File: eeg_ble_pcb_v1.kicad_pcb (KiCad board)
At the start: 2 copper layers, 113 parts, among them J2 Conn_01x10_Socket, J3 Conn_01x10_Socket, J4 2171750001, Q1 FS8205, SW1 SW_Push, U1 STM32WB55RGVx, U2 TP4056-42-ESOP8, U3 ADS1299-4PAGR, U4 TPS61230DRC, U5 TPS63001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

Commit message: small pcb change
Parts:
- moved D2 165.9 mm to (227.6, 44.7)
- moved JP5 158.6 mm to (253.5, 94.7)
- moved Bias1 158.0 mm to (229.6, 96.5)
- moved JP1 158.0 mm to (234.2, 96.5)
- moved JP10 158.0 mm to (243.3, 103.6)
- moved JP11 158.0 mm to (247.9, 103.6)
- moved JP12 158.0 mm to (252.5, 103.6)
- moved JP13 158.0 mm to (229.6, 110.8)
- moved JP14 158.0 mm to (234.2, 110.8)
- moved JP15 158.0 mm to (238.8, 110.8)
- moved JP16 158.0 mm to (243.3, 110.8)
- moved JP17 158.0 mm to (247.9, 110.8)
- moved JP2 158.0 mm to (238.8, 96.5)
- moved JP3 158.0 mm to (243.3, 96.5)
- moved JP4 158.0 mm to (247.9, 96.5)
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
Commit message: PCB ADS1299 and Charging done
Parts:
- moved JP12 238.5 mm to (19.6, 154.6), turned to 90 degrees
- moved JP17 238.2 mm to (19.6, 178.7), turned to 90 degrees
- moved JP11 232.9 mm to (19.6, 149.5), turned to 90 degrees
- moved JP16 232.5 mm to (19.6, 173.9), turned to 90 degrees
- moved JP10 227.5 mm to (19.6, 144.4), turned to 90 degrees
- moved JP15 226.8 mm to (19.6, 169.0), turned to 90 degrees
- moved JP2 224.0 mm to (35.8, 191.4), turned to 180 degrees
- moved JP14 221.2 mm to (19.6, 164.2), turned to 90 degrees
- moved JP5 221.1 mm to (54.6, 191.4), turned to 180 degrees
- moved JP4 219.7 mm to (49.8, 191.4), turned to 180 degrees
- moved JP3 219.7 mm to (45.2, 191.4), turned to 180 degrees
- moved JP13 215.6 mm to (19.6, 159.4), turned to 90 degrees
- moved JP1 215.5 mm to (40.7, 191.4), turned to 180 degrees
- moved Bias1 214.3 mm to (19.6, 139.3), turned to 90 degrees
- moved JP6 191.4 mm to (59.5, 191.4), turned to 180 degrees
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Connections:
- C1 pad 1: OUT- -> VDD
- C10 pad 1: OUT- -> VDD
- C11 pad 1: OUT- -> VDD
- C12 pad 1: OUT- -> VDD
- C13 pad 1: OUT- -> VDD
- C2 pad 1: OUT- -> VDD
- C3 pad 1: OUT- -> VDD
- C38 pad 1: OUT- -> VDD
- C39 pad 1: OUT- -> VDD
- C4 pad 1: OUT- -> VDD
- C5 pad 1: OUT- -> VDD
- C6 pad 1: OUT- -> VDD
- C8 pad 1: OUT- -> VDD
- C9 pad 1: OUT- -> VDD
- J2 pad 6: OUT- -> VDD
- J3 pad 2: OUT- -> VDD
- U1 pad 1: OUT- -> VDD
- U1 pad 13: OUT- -> VDD
- U1 pad 14: OUT- -> VDD
- U1 pad 30: OUT- -> VDD
- U1 pad 33: OUT- -> VDD
- U1 pad 41: OUT- -> VDD
- U1 pad 43: OUT- -> VDD
- U1 pad 44: OUT- -> VDD
- U1 pad 45: OUT- -> VDD
- U1 pad 55: OUT- -> VDD
- U1 pad 68: OUT- -> VDD
- U3 pad 48: OUT- -> VDD
- U3 pad 50: OUT- -> VDD
- U3 pad 52: OUT- -> VDD
- U5 pad 1: OUT- -> VDD
- U5 pad 10: OUT- -> VDD
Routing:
- net OUT-: track 0.00 -> 98.2 mm, vias 0 -> 5
- net +5V: track 0.00 -> 51.8 mm
- net Vout_5: track 0.00 -> 23.6 mm, vias 0 -> 2
- net B-: track 0.00 -> 19.6 mm
- net B+: track 0.00 -> 15.0 mm
- net Net-(U3-VCAP2): track 0.00 -> 12.1 mm
- net Net-(U3-VCAP1): track 0.00 -> 10.2 mm
- net Net-(U6-OD): track 0.00 -> 8.38 mm
- net Net-(U6-OC): track 0.00 -> 8.27 mm
- net Net-(U3-VCAP4): track 0.00 -> 8.21 mm
- net Net-(U3-VREFP): track 0.00 -> 8.18 mm
- net Net-(U6-VCC): track 0.00 -> 7.16 mm
- net Net-(U2-~{STDBY}): track 0.00 -> 4.63 mm
- net Net-(J4-CC2): track 0.00 -> 4.25 mm
- net Net-(J4-CC1): track 0.00 -> 4.14 mm
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
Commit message: stm connections v1
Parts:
- moved JP2 161.4 mm to (183.6, 126.5), turned to -90 degrees
- moved JP1 159.1 mm to (183.6, 121.7), turned to -90 degrees
- moved JP3 157.1 mm to (183.6, 117.1), turned to -90 degrees
- moved JP17 155.6 mm to (170.9, 142.7), turned to 180 degrees
- moved JP4 155.3 mm to (183.6, 112.5), turned to -90 degrees
- moved JP5 153.8 mm to (183.6, 107.7), turned to -90 degrees
- moved JP6 152.5 mm to (183.6, 102.9), turned to -90 degrees
- moved JP7 151.5 mm to (183.6, 97.8), turned to -90 degrees
- moved R17 151.4 mm to (176.0, 126.5), turned to 180 degrees
- moved JP8 150.8 mm to (183.6, 92.7), turned to -90 degrees
- moved JP16 149.8 mm to (166.1, 142.7), turned to 180 degrees
- moved R29 149.7 mm to (170.9, 134.4), turned to 90 degrees
- moved R18 148.9 mm to (176.0, 121.7), turned to 180 degrees
- moved R19 146.8 mm to (176.0, 117.1), turned to 180 degrees
- moved R20 144.9 mm to (176.0, 112.5), turned to 180 degrees
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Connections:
- J2 pad 1: SWCLK -> EXTRA1
- J2 pad 10: EXTRA1 -> unconnected-(J2-Pin_10-Pad10)
- J2 pad 2: SWDIO -> EXTRA2
- J2 pad 3: SWO -> Vout_5
- J2 pad 4: NRST -> VDD
- J2 pad 5: OUT- -> SWO
- J2 pad 6: VDD -> SWCLK
- J2 pad 7: UART_TX -> SWDIO
- J2 pad 9: EXTRA2 -> OUT-
- J3 pad 1: Vout_5 -> VDD
- J3 pad 10: Din_STM -> UART_TX
- J3 pad 2: VDD -> NRST
- J3 pad 3: OUT- -> PWDN_STM
- J3 pad 4: PWDN_STM -> DRDY_STM
- J3 pad 5: DRDY_STM -> CS_STM
- J3 pad 6: Strt_STM -> SCLK_STM
- J3 pad 7: CS_STM -> Dout_STM
- J3 pad 8: SCLK_STM -> Din_STM
- J3 pad 9: Dout_STM -> Strt_STM
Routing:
- net NRST: track 0.00 -> 45.2 mm
- net VDD: track 0.00 -> 42.6 mm
- net EXTRA1: track 0.00 -> 20.4 mm, vias 0 -> 2
- net UART_TX: track 0.00 -> 20.2 mm
- net EXTRA2: track 0.00 -> 19.1 mm
- net Strt_STM: track 0.00 -> 18.3 mm
- net Din_STM: track 0.00 -> 16.8 mm
- net Dout_STM: track 0.00 -> 16.2 mm
- net SCLK_STM: track 0.00 -> 15.1 mm, vias 0 -> 1
- net CS_STM: track 0.00 -> 14.7 mm, vias 0 -> 1
- net PWDN_STM: track 0.00 -> 13.9 mm, vias 0 -> 1
- net DRDY_STM: track 0.00 -> 13.0 mm, vias 0 -> 1
- net UART_RX: track 0.00 -> 12.0 mm, vias 0 -> 1
- net SWCLK: track 0.00 -> 11.1 mm, vias 0 -> 1
- net SWO: track 0.00 -> 11.0 mm, vias 0 -> 1
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
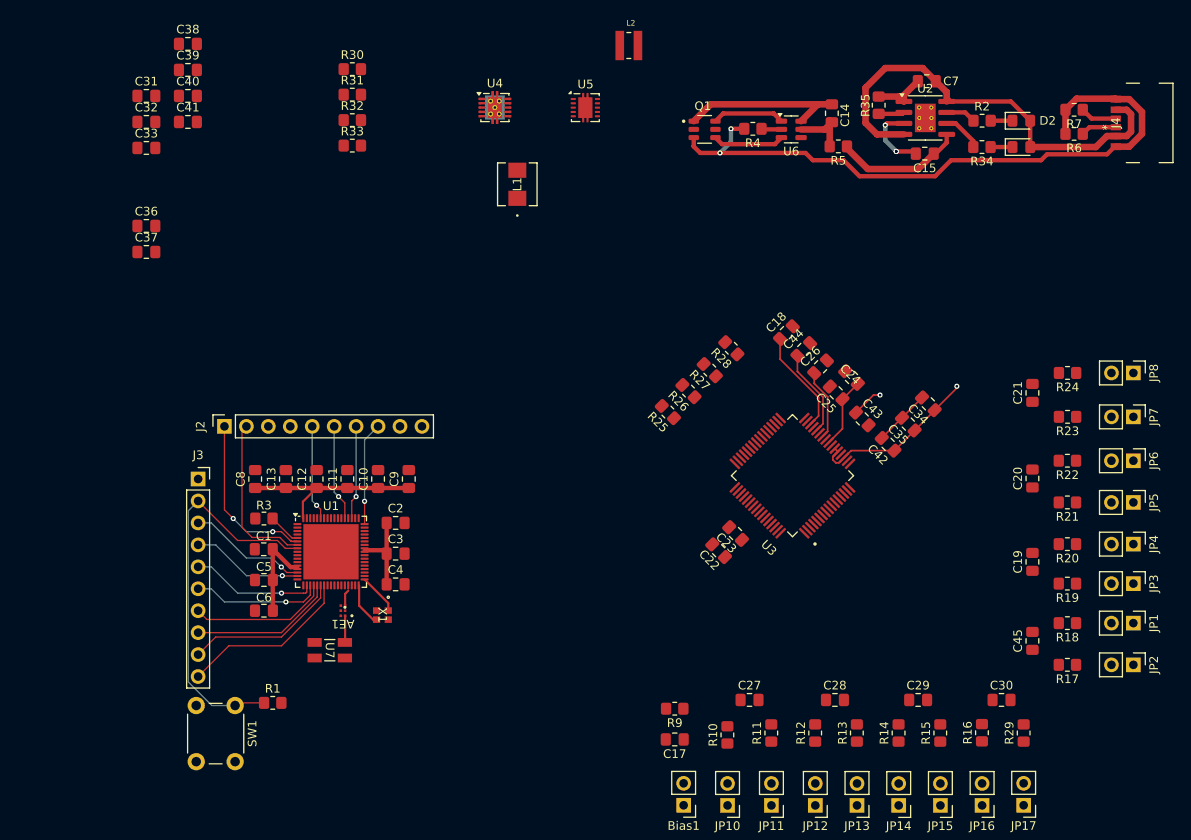
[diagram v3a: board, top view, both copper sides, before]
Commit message: PCB moved around
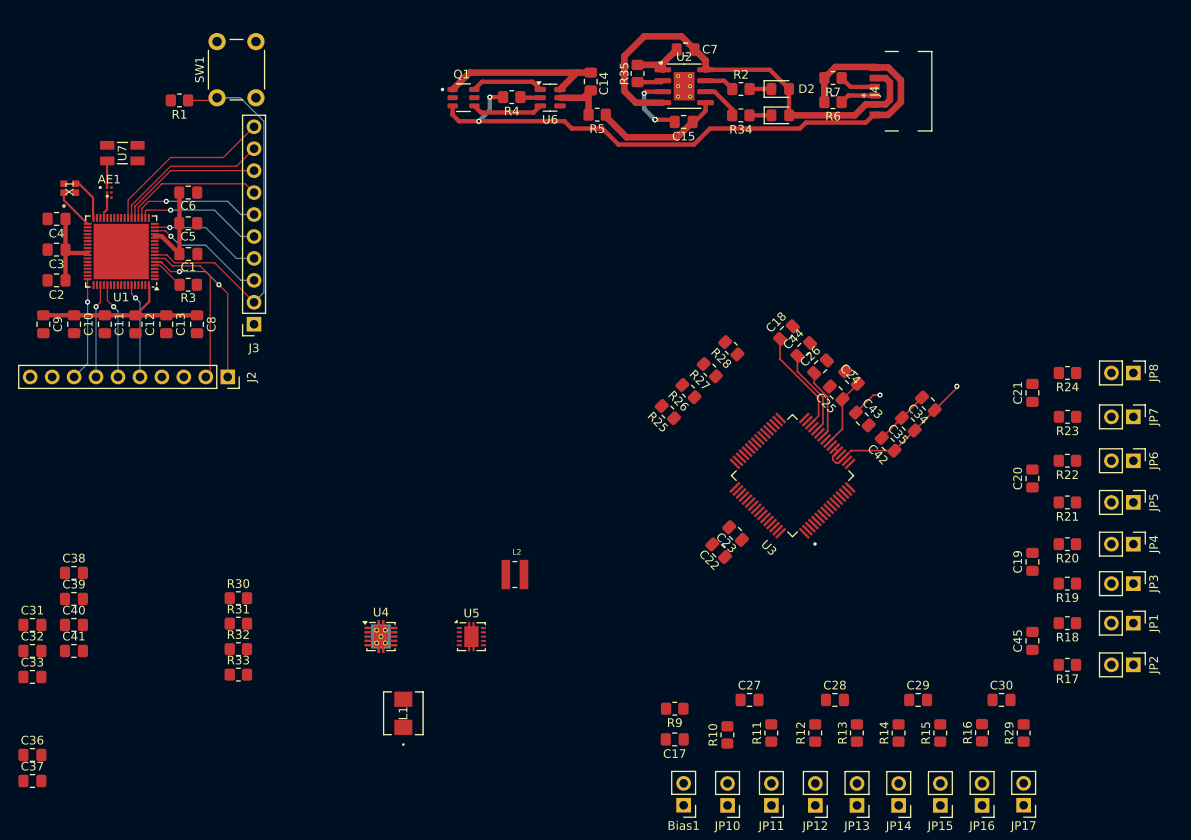
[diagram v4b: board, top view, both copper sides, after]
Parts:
- moved R1 70.6 mm to (73.2, 61.1), turned to 180 degrees
- moved SW1 70.4 mm to (77.6, 60.8), turned to 90 degrees
- moved C33 62.6 mm to (56.2, 127.9)
- moved C36 62.6 mm to (56.2, 136.9)
- moved C37 62.6 mm to (56.2, 139.9)
- moved C39 62.6 mm to (61.0, 118.9)
- moved L1 62.6 mm to (99.1, 132.1)
- moved R30 62.6 mm to (80.0, 118.8)
- moved R31 62.6 mm to (80.0, 121.7)
- moved R32 62.6 mm to (80.0, 124.7)
- moved U4 62.6 mm to (96.5, 123.2)
- moved C31 62.6 mm to (56.2, 121.9)
- moved C32 62.6 mm to (56.2, 124.9)
- moved C38 62.6 mm to (61.0, 115.8)
- moved C40 62.6 mm to (61.0, 121.9)
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
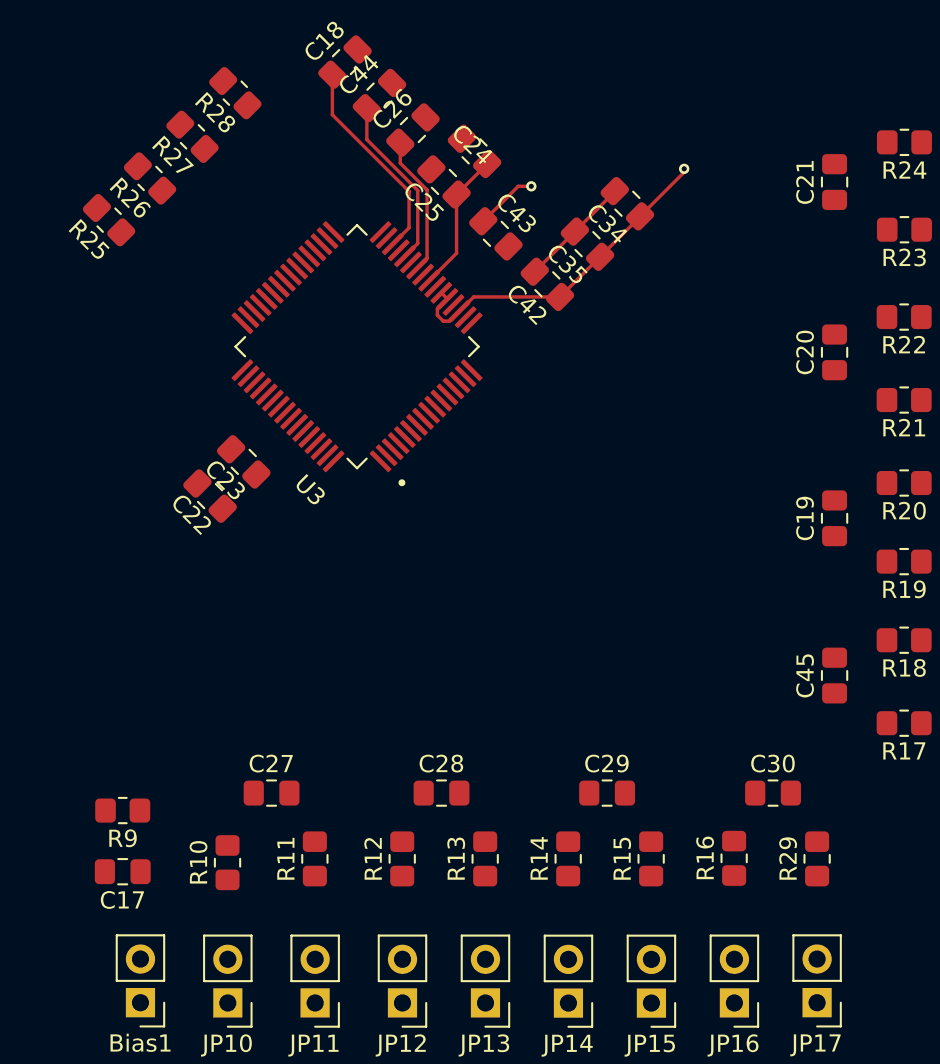
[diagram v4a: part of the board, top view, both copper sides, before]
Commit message: Input Cap change and PCB connections
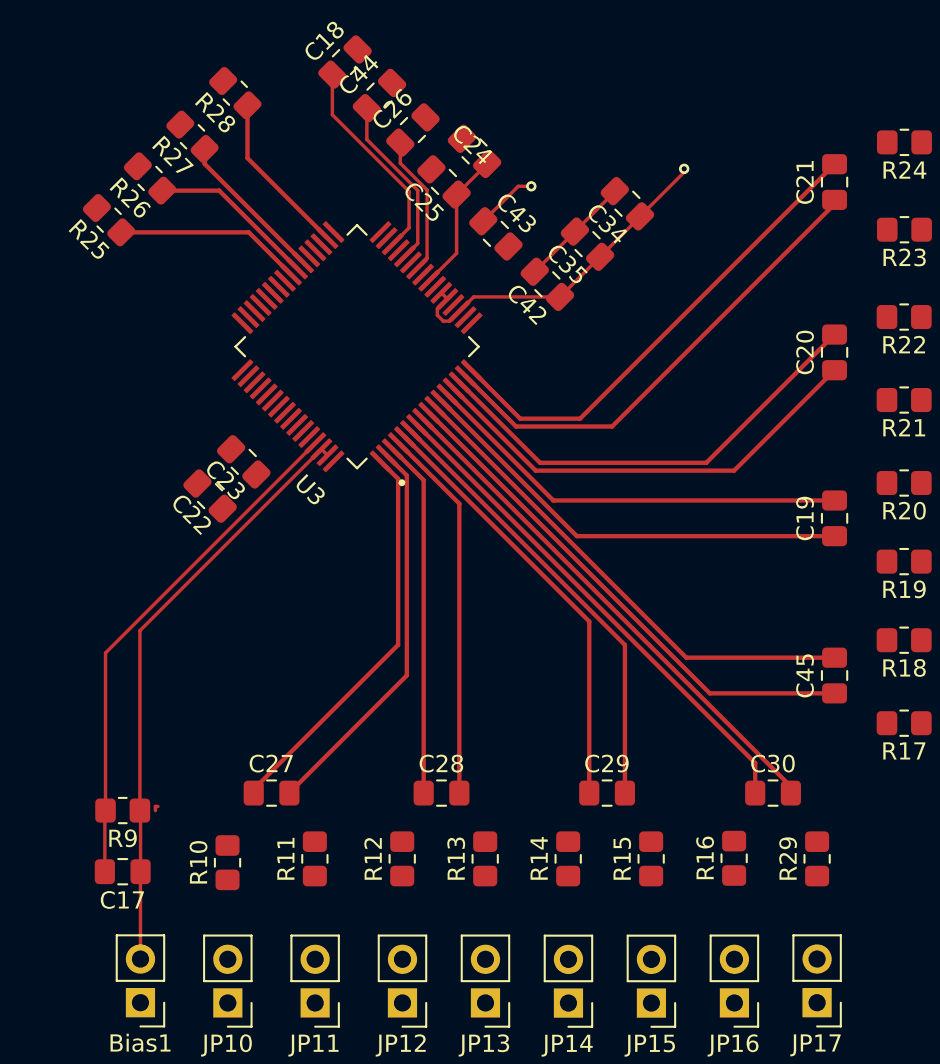
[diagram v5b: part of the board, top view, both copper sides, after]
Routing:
- net Net-(Bias1-B): track 0.00 -> 34.5 mm
- net Net-(U3-IN5P): track 0.00 -> 30.6 mm
- net Net-(U3-IN4N): track 0.00 -> 30.3 mm
- net Net-(U3-BIASINV): track 0.00 -> 30.0 mm
- net Net-(U3-IN5N): track 0.00 -> 29.6 mm
- net Net-(U3-IN4P): track 0.00 -> 29.3 mm
- net Net-(U3-IN1P): track 0.00 -> 28.4 mm
- net Net-(U3-IN1N): track 0.00 -> 28.3 mm
- net Net-(U3-IN2P): track 0.00 -> 26.8 mm
- net Net-(U3-IN2N): track 0.00 -> 26.6 mm
- net Net-(U3-IN6P): track 0.00 -> 26.2 mm
- net Net-(U3-IN3N): track 0.00 -> 26.1 mm
- net Net-(U3-IN6N): track 0.00 -> 25.2 mm
- net Net-(U3-IN3P): track 0.00 -> 25.1 mm
- net Net-(U3-IN8P): track 0.00 -> 23.8 mm
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
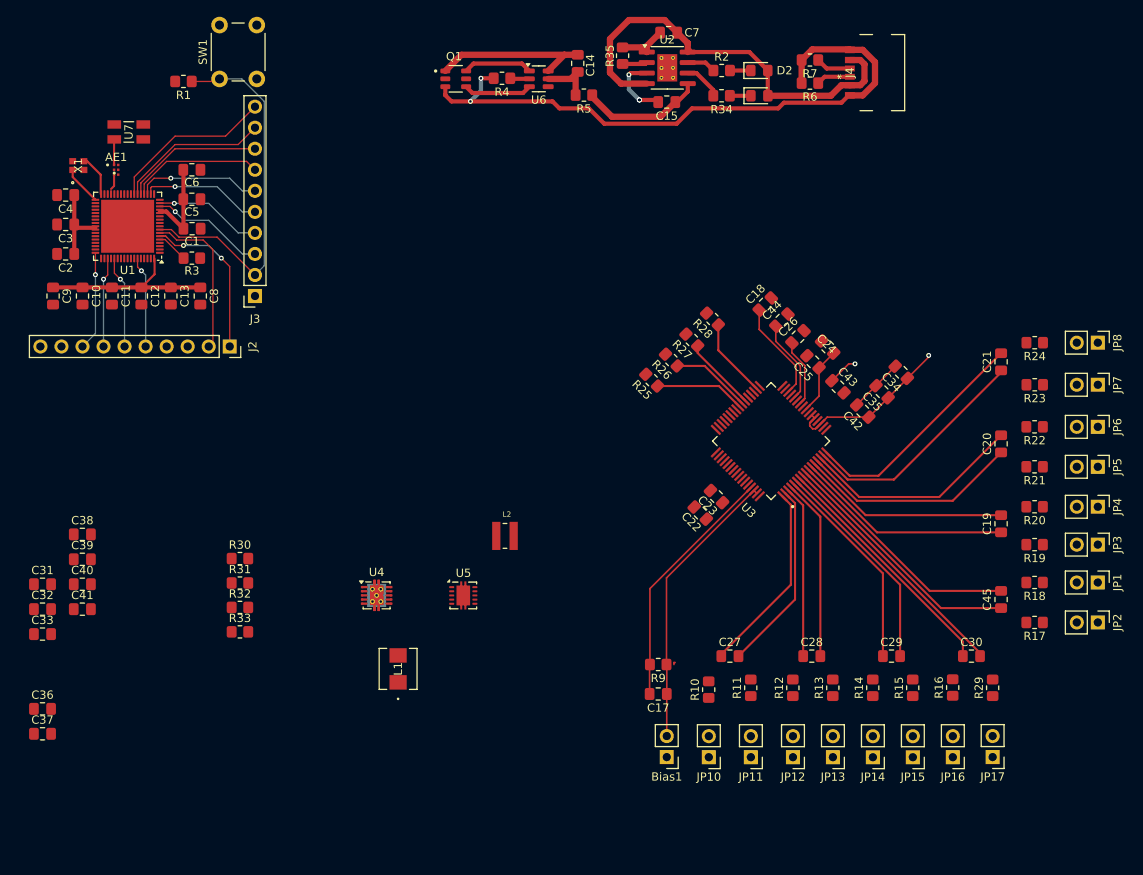
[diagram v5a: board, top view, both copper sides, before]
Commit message: Full Differential PCB done
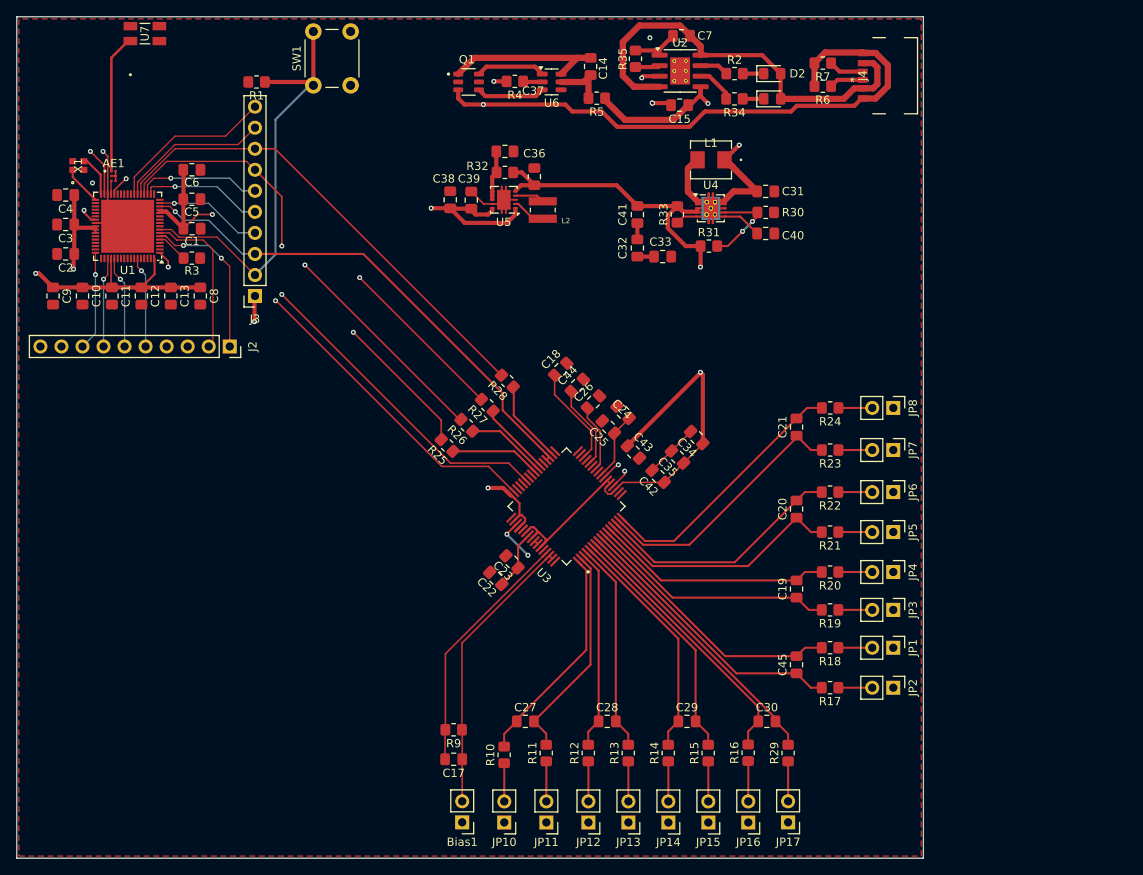
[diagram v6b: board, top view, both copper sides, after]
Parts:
- moved C31 99.4 mm to (143.5, 74.4)
- moved C40 92.8 mm to (143.5, 79.5)
- moved C37 89.8 mm to (112.0, 69.6)
- moved C33 87.7 mm to (131.1, 82.3)
- moved C36 87.5 mm to (115.6, 72.6), turned to 90 degrees
- moved C32 84.0 mm to (128.0, 81.3), turned to -90 degrees
- moved C41 82.2 mm to (128.0, 77.2), turned to -90 degrees
- moved R30 76.0 mm to (143.5, 77.0)
- moved R33 73.0 mm to (132.9, 77.2), turned to 90 degrees
- moved L1 72.2 mm to (136.9, 70.6), turned to 180 degrees
- moved R31 69.7 mm to (136.7, 81.0)
- moved C39 63.9 mm to (108.0, 75.5), turned to 90 degrees
- moved U4 61.8 mm to (136.9, 76.5)
- moved R32 61.5 mm to (112.0, 72.1), turned to 180 degrees
- moved C38 60.0 mm to (105.4, 75.4), turned to 90 degrees
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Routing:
- net Vout_5: track 23.6 -> 172.9 mm
- net VDD: track 42.6 -> 100.0 mm, vias 0 -> 10
- net Dout_STM: track 16.2 -> 71.3 mm, vias 0 -> 2
- net DRDY_STM: track 13.0 -> 60.6 mm, vias 1 -> 2
- net PWDN_STM: track 13.9 -> 61.3 mm
- net Strt_STM: track 18.3 -> 63.4 mm, vias 0 -> 1
- net Din_STM: track 16.8 -> 57.9 mm
- net SCLK_STM: track 15.1 -> 54.4 mm, vias 1 -> 2
- net OUT-: track 98.2 -> 135.0 mm, vias 5 -> 12
- net CS_STM: track 14.7 -> 50.2 mm, vias 1 -> 2
- net B+: track 15.0 -> 39.1 mm, vias 0 -> 2
- net Net-(AE1-OUT): track 3.09 -> 17.0 mm
- net Net-(U4-FB): track 0.00 -> 10.7 mm, vias 0 -> 2
- net NRST: track 45.2 -> 52.8 mm
- net Net-(L1-Pad2): track 0.00 -> 7.47 mm
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- added copper zone on F.Cu, net OUT-
- added copper zone on In1.Cu, net OUT-
- added copper zone on In2.Cu, net VDD
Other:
- board outline added: 109.5 x 101.6 mm
- copper layers 2 -> 4
- board text added: "24 MAR 2026"
- board text added: "Full PCB for Differential EEG set-up"
